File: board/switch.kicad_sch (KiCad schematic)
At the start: 23 parts, among them IC1 RTL8305NB-CG, Y1 25Mhz

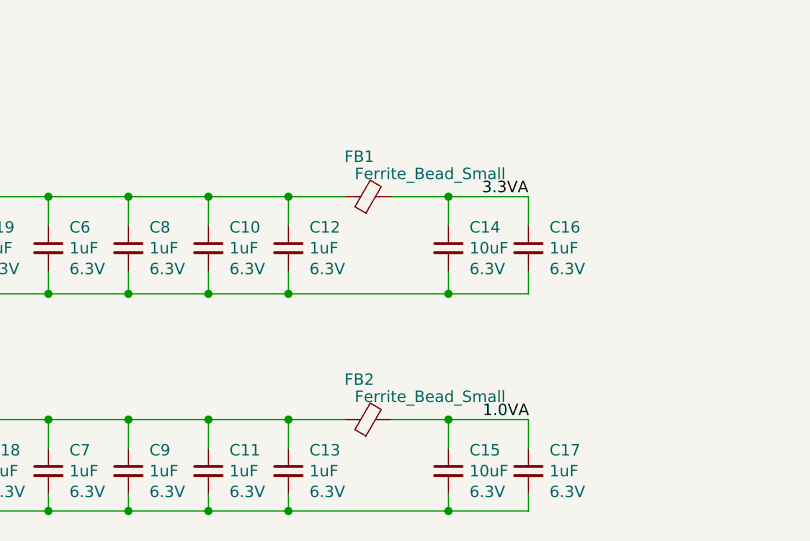
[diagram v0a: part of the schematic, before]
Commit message: added lcsc numbers and updated I2C connector
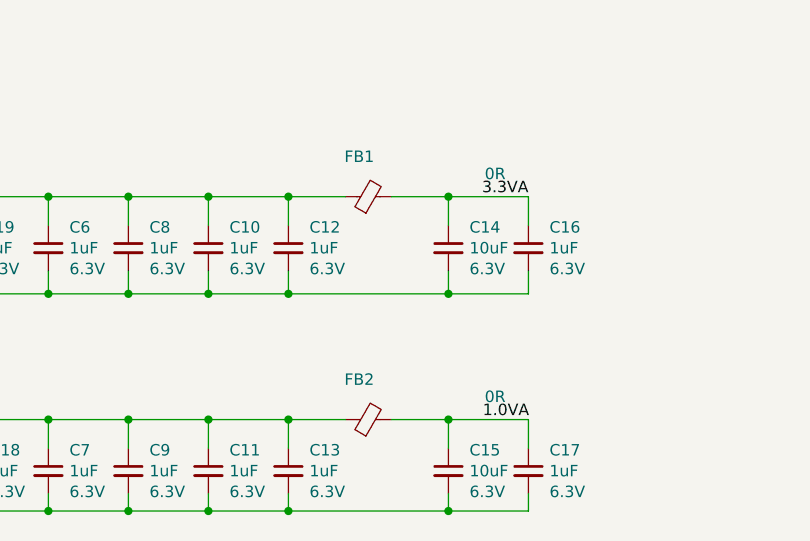
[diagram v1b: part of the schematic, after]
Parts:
- C10, C11, C12, C13, C16, C17, C18, C19, C6, C7, C8, C9: lcsc (none) -> C52923
- C14, C15, C4, C5: lcsc (none) -> C15525
- C2, C3: lcsc (none) -> C1555
- FB1, FB2: value Ferrite_Bead_Small -> 0R; lcsc (none) -> C21189
- IC1: lcsc (none) -> C52146
- R2: footprint Resistor_SMD:R_0603_1608Metric -> Resistor_SMD:R_0402_1005Metric; lcsc (none) -> C25884
- Y1: lcsc (none) -> C9006
